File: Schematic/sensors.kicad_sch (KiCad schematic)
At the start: 0 parts

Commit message: Mostly finallized PCB
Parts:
- added J18: LASER, Connector_JST:JST_VH_B2P-VH-B_1x02_P3.96mm_Vertical, symbol Connector_Generic:Conn_01x02
- added J19: LDR, Connector_JST:JST_VH_B2P-VH-B_1x02_P3.96mm_Vertical, symbol Connector_Generic:Conn_01x02
- added R2: 10k, Resistor_SMD:R_1206_3216Metric_Pad1.30x1.75mm_HandSolder, symbol Device:R
- added R3: 100, Resistor_SMD:R_1206_3216Metric_Pad1.30x1.75mm_HandSolder, symbol Device:R
- added R4, R5: 1k, Resistor_SMD:R_1206_3216Metric_Pad1.30x1.75mm_HandSolder, symbol Device:R
- added RV1: R_Potentiometer, Potentiometer_THT:Potentiometer_Vishay_148-149_Single_Vertical, symbol Device:R_Potentiometer
- added U1: LM358, Package_DIP:DIP-8_W7.62mm, symbol Amplifier_Operational:LM358
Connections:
- new net: J19.2 (Pin_2), R2.2, U1.2 (-)
- new net: R4.2, R5.1, U1.5 (+)
- new net: J18.2 (Pin_2), R3.1
- new net: U1.6 (-), U1.7
- new net: RV1.2, U1.3 (+)
- new net +5V: J19.1 (Pin_1), R3.2, R4.1, RV1.3, U1.8 (V+)
- new net GND: J18.1 (Pin_1), R2.1, R5.2, RV1.1, U1.4 (V-)
- new net PB14: U1.1

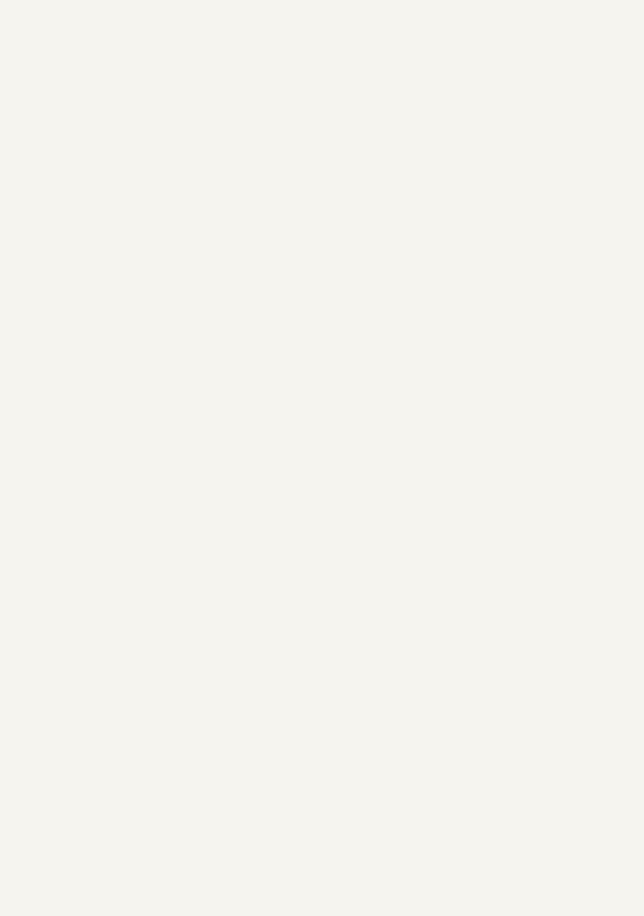
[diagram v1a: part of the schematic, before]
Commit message: Added images
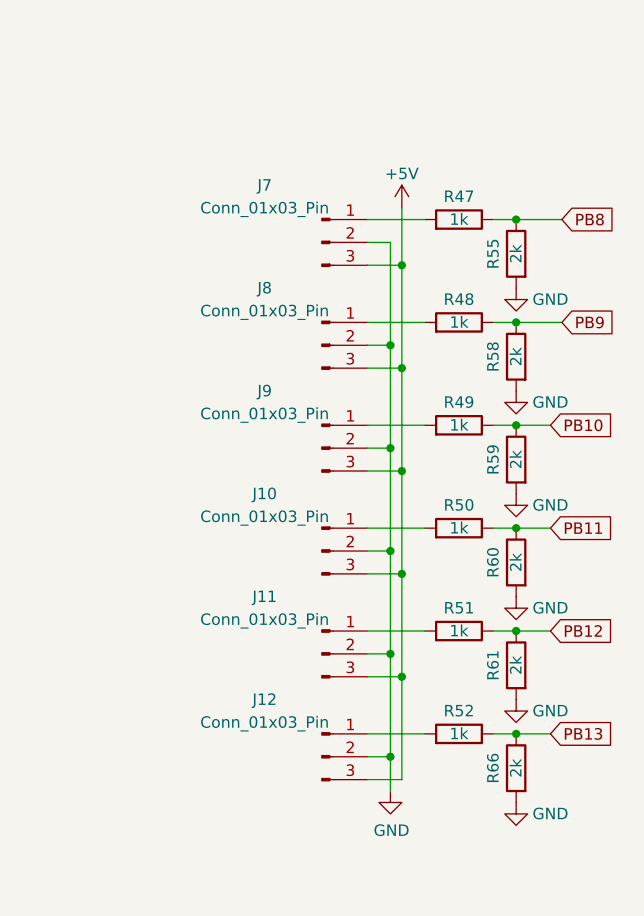
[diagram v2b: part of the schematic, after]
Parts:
- added J10, J11, J12, J7, J8, J9: Conn_01x03_Pin, Connector_JST:JST_VH_B3P-VH_1x03_P3.96mm_Vertical, symbol Connector:Conn_01x03_Pin
- added R47, R48, R49, R50, R51, R52: 1k, Resistor_SMD:R_1206_3216Metric_Pad1.30x1.75mm_HandSolder, symbol Device:R
- added R55, R58, R59, R60, R61, R66: 2k, Resistor_SMD:R_1206_3216Metric_Pad1.30x1.75mm_HandSolder, symbol Device:R
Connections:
- net +5V: now also J10.3 (Pin_3), J11.3 (Pin_3), J12.3 (Pin_3), J7.3 (Pin_3), J8.3 (Pin_3), J9.3 (Pin_3)
- net GND: now also J10.2 (Pin_2), J11.2 (Pin_2), J12.2 (Pin_2), J7.2 (Pin_2), J8.2 (Pin_2), J9.2 (Pin_2), R55.2, R58.2, R59.2, R60.2, R61.2, R66.2
- new net: J10.1 (Pin_1), R50.2
- new net: J9.1 (Pin_1), R49.2
- new net: J7.1 (Pin_1), R47.2
- new net: J12.1 (Pin_1), R52.2
- new net: J8.1 (Pin_1), R48.2
- new net: J11.1 (Pin_1), R51.2
- new net PB10: R49.1, R59.1
- new net PB11: R50.1, R60.1
- new net PB12: R51.1, R61.1
- new net PB13: R52.1, R66.1
- new net PB8: R47.1, R55.1
- new net PB9: R48.1, R58.1

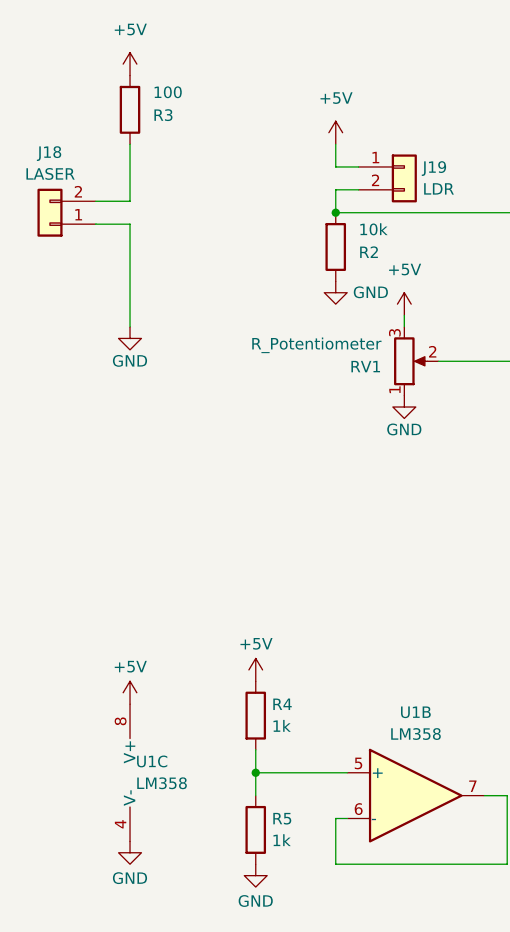
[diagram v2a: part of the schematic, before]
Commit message: Added Cap to osilator, and fixed posible issues with signals near it.
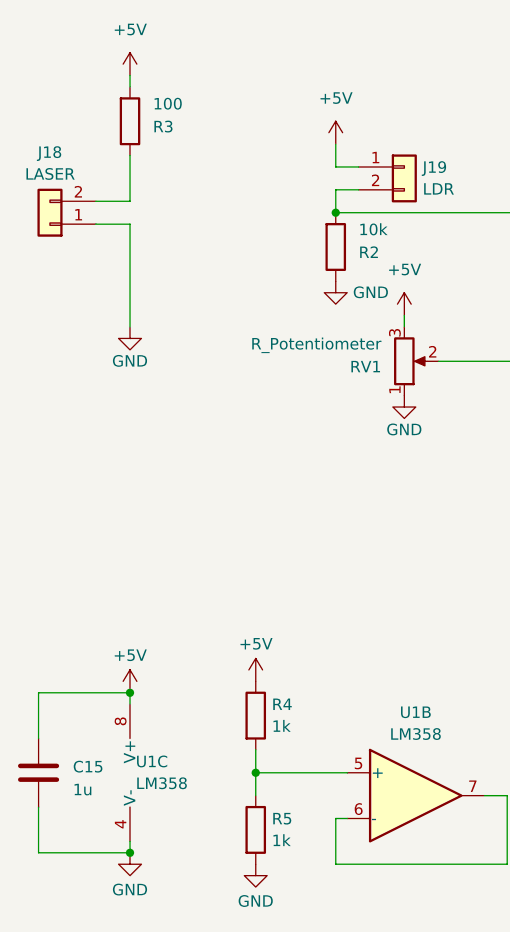
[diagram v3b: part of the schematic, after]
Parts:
- added C15: 1u, Capacitor_SMD:C_1206_3216Metric_Pad1.33x1.80mm_HandSolder, symbol Device:C
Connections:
- net +5V: now also C15.1
- net GND: now also C15.2
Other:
- moved on the sheet: R3
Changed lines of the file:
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@@
   (junction (at 201.93 76.2) (diameter 0) (color 0 0 0 0)
   )
+  (junction (at 66.04 128.27) (diameter 0) (color 0 0 0 0)
+  )
   (junction (at 214.63 71.12) (diameter 0) (color 0 0 0 0)
   )
@@
   (junction (at 201.93 64.77) (diameter 0) (color 0 0 0 0)
   )
+  (junction (at 66.04 110.49) (diameter 0) (color 0 0 0 0)
+  )
   (junction (at 214.63 82.55) (diameter 0) (color 0 0 0 0)
   )
@@
     (stroke (width 0) (type default))
   )
+  (wire (pts (xy 66.04 128.27) (xy 66.04 127))
+    (stroke (width 0) (type default))
+  )
   (wire (pts (xy 200.66 119.38) (xy 198.12 119.38))
     (stroke (width 0) (type default))
@@
     (stroke (width 0) (type default))
   )
+  (wire (pts (xy 55.88 123.19) (xy 55.88 128.27))
+    (stroke (width 0) (type default))
+  )
+  (wire (pts (xy 55.88 110.49) (xy 55.88 115.57))
+    (stroke (width 0) (type default))
+  )
   (wire (pts (xy 200.66 96.52) (xy 200.66 107.95))
     (stroke (width 0) (type default))
@@
     (stroke (width 0) (type default))
   )
+  (wire (pts (xy 55.88 128.27) (xy 66.04 128.27))
+    (stroke (width 0) (type default))
+  )
   (wire (pts (xy 110.49 57.15) (xy 110.49 58.42))
     (stroke (width 0) (type default))
@@
     (stroke (width 0) (type default))
   )
+  (wire (pts (xy 55.88 110.49) (xy 66.04 110.49))
+    (stroke (width 0) (type default))
+  )
   (wire (pts (xy 214.63 116.84) (xy 218.44 116.84))
     (stroke (width 0) (type default))
@@
     (stroke (width 0) (type default))
   )
+  (wire (pts (xy 66.04 43.18) (xy 66.04 41.91))
+    (stroke (width 0) (type default))
+  )
   (wire (pts (xy 198.12 59.69) (xy 204.47 59.69))
     (stroke (width 0) (type default))
@@
     (stroke (width 0) (type default))
   )
+  (wire (pts (xy 66.04 110.49) (xy 66.04 111.76))
+    (stroke (width 0) (type default))
+  )
   (wire (pts (xy 198.12 116.84) (xy 204.47 116.84))
     (stroke (width 0) (type default))
@@
     (stroke (width 0) (type default))
   )
-  (wire (pts (xy 66.04 55.88) (xy 66.04 49.53))
+  (wire (pts (xy 66.04 55.88) (xy 66.04 50.8))
     (stroke (width 0) (type default))
   )
@@
     )
   )
-  (symbol (lib_id "power:+5V") (at 66.04 111.76 0) (unit 1)
-    (in_bom yes) (on_board yes) (dnp no) (fields_autoplaced)
-    (property "Reference" "#PWR06" (at 66.04 115.57 0)
-      (effects (font (size 1.27 1.27)) hide)
-    )
-    (property "Value" "+5V" (at 66.04 107.6269 0)
-      (effects (font (size 1.27 1.27)))
-    )
-    (property "Footprint" "" (at 66.04 111.76 0)
-      (effects (font (size 1.27 1.27)) hide)
-    )
-    (property "Datasheet" "" (at 66.04 111.76 0)
+  (symbol (lib_id "power:+5V") (at 66.04 110.49 0) (mirror y) (unit 1)
+    (in_bom yes) (on_board yes) (dnp no)
+    (property "Reference" "#PWR06" (at 66.04 114.3 0)
+      (effects (font (size 1.27 1.27)) hide)
+    )
+    (property "Value" "+5V" (at 66.04 106.3569 0)
+      (effects (font (size 1.27 1.27)))
+    )
+    (property "Footprint" "" (at 66.04 110.49 0)
+      (effects (font (size 1.27 1.27)) hide)
+    )
+    (property "Datasheet" "" (at 66.04 110.49 0)
       (effects (font (size 1.27 1.27)) hide)
     )
@@
     )
   )
-  (symbol (lib_id "Device:R") (at 66.04 45.72 0) (mirror x) (unit 1)
-    (in_bom yes) (on_board yes) (dnp no) (fields_autoplaced)
-    (property "Reference" "R3" (at 68.58 46.355 0)
+  (symbol (lib_id "Device:R") (at 66.04 46.99 0) (mirror x) (unit 1)
+    (in_bom yes) (on_board yes) (dnp no) (fields_autoplaced)
+    (property "Reference" "R3" (at 68.58 47.625 0)
       (effects (font (size 1.27 1.27)) (justify left))
     )
-    (property "Value" "100" (at 68.58 43.815 0)
+    (property "Value" "100" (at 68.58 45.085 0)
       (effects (font (size 1.27 1.27)) (justify left))
     )
-    (property "Footprint" "Resistor_SMD:R_1206_3216Metric_Pad1.30x1.75mm_HandSolder" (at 64.262 45.72 90)
-      (effects (font (size 1.27 1.27)) hide)
-    )
-    (property "Datasheet" "~" (at 66.04 45.72 0)
+    (property "Footprint" "Resistor_SMD:R_1206_3216Metric_Pad1.30x1.75mm_HandSolder" (at 64.262 46.99 90)
+      (effects (font (size 1.27 1.27)) hide)
+    )
+    (property "Datasheet" "~" (at 66.04 46.99 0)
       (effects (font (size 1.27 1.27)) hide)
     )
@@
     )
   )
-  (symbol (lib_id "power:GND") (at 66.04 127 0) (unit 1)
-    (in_bom yes) (on_board yes) (dnp no) (fields_autoplaced)
-    (property "Reference" "#PWR07" (at 66.04 133.35 0)
-      (effects (font (size 1.27 1.27)) hide)
-    )
-    (property "Value" "GND" (at 66.04 131.1331 0)
-      (effects (font (size 1.27 1.27)))
-    )
-    (property "Footprint" "" (at 66.04 127 0)
-      (effects (font (size 1.27 1.27)) hide)
-    )
-    (property "Datasheet" "" (at 66.04 127 0)
+  (symbol (lib_id "power:GND") (at 66.04 128.27 0) (unit 1)
+    (in_bom yes) (on_board yes) (dnp no) (fields_autoplaced)
+    (property "Reference" "#PWR07" (at 66.04 134.62 0)
+      (effects (font (size 1.27 1.27)) hide)
+    )
+    (property "Value" "GND" (at 66.04 132.4031 0)
+      (effects (font (size 1.27 1.27)))
+    )
+    (property "Footprint" "" (at 66.04 128.27 0)
+      (effects (font (size 1.27 1.27)) hide)
+    )
+    (property "Datasheet" "" (at 66.04 128.27 0)
       (effects (font (size 1.27 1.27)) hide)
     )
@@
         )
       )
+    )
+  )
+  (symbol (lib_id "Device:C") (at 55.88 119.38 0) (unit 1)
+    (in_bom yes) (on_board yes) (dnp no) (fields_autoplaced)
+    (property "Reference" "C15" (at 59.69 118.745 0)
+      (effects (font (size 1.27 1.27)) (justify left))
+    )
+    (property "Value" "1u" (at 59.69 121.285 0)
+      (effects (font (size 1.27 1.27)) (justify left))
+    )
+    (property "Footprint" "Capacitor_SMD:C_1206_3216Metric_Pad1.33x1.80mm_HandSolder" (at 56.8452 123.19 0)
+      (effects (font (size 1.27 1.27)) hide)
+    )
+    (property "Datasheet" "~" (at 55.88 119.38 0)
+      (effects (font (size 1.27 1.27)) hide)
+    )
+    (pin "1")
+    (pin "2")
+    (instances
+      (project "Schematic"
+        (path "/ced54cd9-3b34-40e4-aa66-964aaab81b0a/575551e4-af3a-490e-80f8-c842b6f0dfe5"
+          (reference "C15") (unit 1)
+        )
+      )

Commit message: Lab fixes
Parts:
- added C17, C18, C19, C20, C21, C22: 10n, Capacitor_SMD:C_1206_3216Metric_Pad1.33x1.80mm_HandSolder, symbol Device:C
- added J13: Conn_01x03_Pin, Connector_PinHeader_2.54mm:PinHeader_1x03_P2.54mm_Vertical, symbol Connector:Conn_01x03_Pin
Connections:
- net +5V: now also J13.1 (Pin_1); no longer J10.3 (Pin_3), J11.3 (Pin_3), J12.3 (Pin_3), J7.3 (Pin_3), J8.3 (Pin_3), J9.3 (Pin_3)
- net GND: now also C17.2, C18.2, C19.2, C20.2, C21.2, C22.2
- net PB10: now also C20.1
- net PB11: now also C19.1
- net PB12: now also C18.1
- net PB13: now also C17.1
- net PB8: now also C22.1
- net PB9: now also C21.1
- new net +3V0: J13.3 (Pin_3)
- new net Vsens: J10.3 (Pin_3), J11.3 (Pin_3), J12.3 (Pin_3), J13.2 (Pin_2), J7.3 (Pin_3), J8.3 (Pin_3), J9.3 (Pin_3)

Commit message: relabeld all of the components so they have more resonable numbers
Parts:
- renumbered C15 to C16, C22 to C17, C21 to C18, C20 to C19, C19 to C20, C18 to C21, C17 to C22, J13 to J10, J7 to J11, J8 to J12, J9 to J13, J10 to J14, J11 to J15, J12 to J16, J18 to J8, J19 to J9

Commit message: fixed LM385 not having voltage div, and ploted plots.
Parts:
- added R47: 1k, Resistor_SMD:R_1206_3216Metric_Pad1.30x1.75mm_HandSolder, symbol Device:R
- added R55: 2k, Resistor_SMD:R_1206_3216Metric_Pad1.30x1.75mm_HandSolder, symbol Device:R
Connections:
- net GND: now also R55.2
- net PB14: now also R47.1, R55.1; no longer U1.1
- new net: R47.2, U1.1
